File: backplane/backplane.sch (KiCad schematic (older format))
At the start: 57 parts, among them J1 Conn_PCB1, J10 Conn_SSR_INPUT, J12 Conn_SSR_PCB2, J13 Conn_01x05, J14 LCD_MCU_CONNECTOR, J15 Screw_Terminal_AQ_2, J16 Screw_Terminal_AQ_1, J17 Screw_Terminal_O3_1, J18 Conn_TO_ION_AIR, J19 Conn_01x08, J2 Conn_PCB2, J20 FAN_CONNECTOR, J21 PERFUME_CONNECTOR, J22 LED_STRIP_CONNECTOR, J23 PCB1_COMM_CONNECTOR, J24 Conn_01x08, J25 PCB1_ALARM, J26 CONNECTOR, J27 UART2, J28 TEST, J29 UART3, J3 Conn_FAN_48V_SOURCE, J30 CONNECTOR, J31 LCD_MCU_CONNECTOR, J32 UART2, J33 UART3, J34 232_TEST_POINT, J35 UART_TEST_POINT, J36 MCU_UART_TEST_POINT, J37 FAN_TEST_POINT, J4 CONNECTOR, J5 Conn_SSR_POWER_SOURCE, J6 Conn_MCU_5V_SOURCE, J7 Conn_humidity_sensor_terminal, J8 Conn_flow_sensor_terminal, J9 Conn_SSR_5V_INPUT, Q4 2n3904, Q5 2n3904, Q6 2n3904, U1 BLUEPILL, U2 MAX3232_MODULE

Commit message: remove uart, 232 circuit,
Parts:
- removed D1, D2, D3, D5: LED, LED_THT:LED_D3.0mm_Clear, symbol Device:LED
- removed J32: UART2, backplate:PhoenixContact_MCV_1,5_2-G-3.5_1x02_P3.50mm_Vertical_handsolder, symbol bluepill:Conn_01x02
- removed J33: UART3, backplate:PhoenixContact_MCV_1,5_2-G-3.5_1x03_P3.50mm_Vertical_handsolder, symbol bluepill:Conn_01x03
- removed J34: 232_TEST_POINT, backplate:Pin_Header_Straight_1x02_Pitch2.54mm, symbol bluepill:Conn_01x02
- removed J35: UART_TEST_POINT, backplate:Pin_Header_Straight_1x02_Pitch2.54mm, symbol bluepill:Conn_01x02
- removed J36: MCU_UART_TEST_POINT, backplate:Pin_Header_Straight_1x02_Pitch2.54mm, symbol bluepill:Conn_01x02
- removed Q4, Q5, Q6: 2n3904, backplate:TO-92L_HandSolder, symbol Transistor_BJT:2N3904
- removed R11, R7, R8, R9: 330, backplate:R_1206_3216Metric_Pad1.42x1.75mm_HandSolder, symbol Device:R
- removed R12, R13, R14: 120, backplate:R_1206_3216Metric_Pad1.42x1.75mm_HandSolder, symbol Device:R
- removed R15, R16, R17: 0, backplate:R_1206_3216Metric_Pad1.42x1.75mm_HandSolder, symbol Device:R
- removed U2: MAX3232_MODULE, backplate:MAX3232_MOEULE_handsolder, symbol bluepill:MAX3232_MODULE
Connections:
- wire segments 299 -> 233

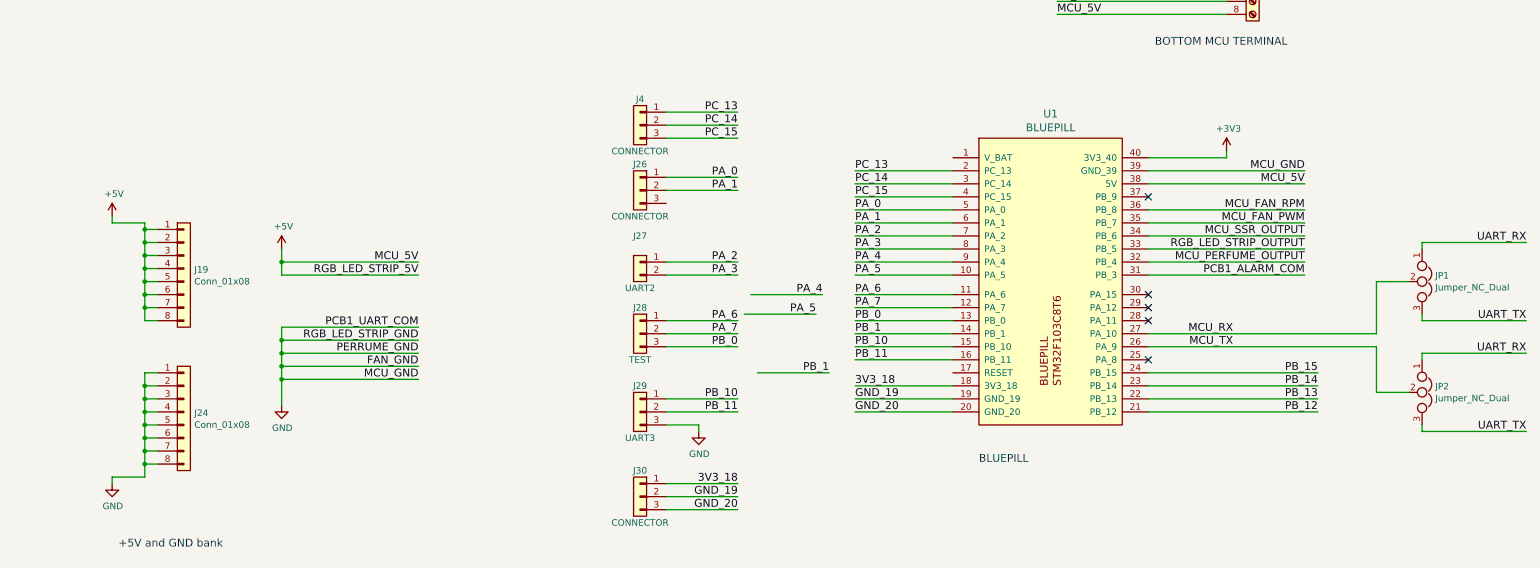
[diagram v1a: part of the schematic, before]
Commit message: remove stm32,
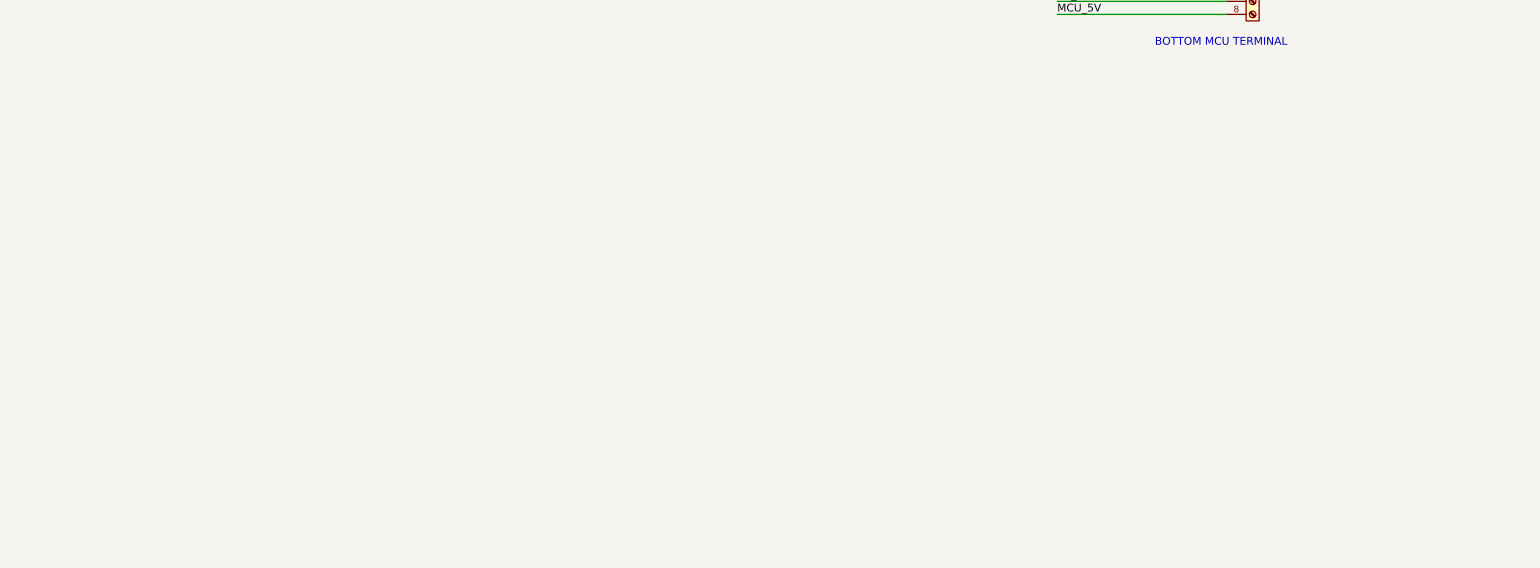
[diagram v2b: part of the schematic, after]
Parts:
- removed J19, J24: Conn_01x08, backplate:PinHeader_1x08_P2.54mm_Vertical_handsolder, symbol Connector_Generic:Conn_01x08
- removed J26, J30, J4: CONNECTOR, backplate:PhoenixContact_MCV_1,5_2-G-3.5_1x03_P3.50mm_Vertical_handsolder, symbol bluepill:Conn_01x03
- removed J27: UART2, backplate:PhoenixContact_MCV_1,5_2-G-3.5_1x02_P3.50mm_Vertical_handsolder, symbol bluepill:Conn_01x02
- removed J28: TEST, backplate:PhoenixContact_MCV_1,5_2-G-3.5_1x03_P3.50mm_Vertical_handsolder, symbol bluepill:Conn_01x03
- removed J29: UART3, backplate:PhoenixContact_MCV_1,5_2-G-3.5_1x03_P3.50mm_Vertical_handsolder, symbol bluepill:Conn_01x03
- removed JP1, JP2: Jumper_NC_Dual, backplate:SolderJumper-3_P1.3mm_Open_RoundedPad1.0x1.5mm, symbol Device:Jumper_NC_Dual
- removed U1: BLUEPILL, backplate:DIP-40_W15.24mm_Socket_LongPads_handsolder, symbol bluepill:BLUEPILL
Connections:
- net +5V: no longer J14.8 (Pin_8), J22.1 (Pin_1), J31.8 (Pin_8), J6.1 (Pin_1)
- net GND: no longer J14.1 (Pin_1), J20.2 (Pin_2), J21.2 (Pin_2), J22.3 (Pin_3), J23.1 (Pin_1), J3.2 (Pin_2), J31.1 (Pin_1), J37.2 (Pin_2), J6.2 (Pin_2)
- new net FAN_GND: J20.2 (Pin_2), J3.2 (Pin_2), J37.2 (Pin_2)
- new net MCU_5V: J14.8 (Pin_8), J31.8 (Pin_8), J6.1 (Pin_1)
- new net MCU_GND: J14.1 (Pin_1), J31.1 (Pin_1), J6.2 (Pin_2)
- new net PCB1_UART_COM: J23.1 (Pin_1)
- new net PERRUME_GND: J21.2 (Pin_2)
- new net RGB_LED_STRIP_5V: J22.1 (Pin_1)
- new net RGB_LED_STRIP_GND: J22.3 (Pin_3)
- no-connect marks 6 -> 1
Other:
- note removed: "+5V and GND bank"
- note removed: "BLUEPILL"

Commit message: remove stm32,
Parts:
- removed J14: LCD_MCU_CONNECTOR, backplate:TE_84952-8_1x08-1MP_P1.0mm_Horizontal, symbol Connector_Generic:Conn_01x08
- removed J20: FAN_CONNECTOR, backplate:PhoenixContact_MCV_1,5_4-G-3.5_1x04_P3.50mm_Vertical_handsolder, symbol Connector_Generic:Conn_01x04
- removed J21: PERFUME_CONNECTOR, backplate:PhoenixContact_MCV_1,5_2-G-3.5_1x02_P3.50mm_Vertical_handsolder, symbol bluepill:Conn_01x02
- removed J22: LED_STRIP_CONNECTOR, backplate:PhoenixContact_MCV_1,5_2-G-3.5_1x03_P3.50mm_Vertical_handsolder, symbol bluepill:Conn_01x03
- removed J3: Conn_FAN_48V_SOURCE, backplate:PhoenixContact_MCV_1,5_2-G-3.5_1x02_P3.50mm_Vertical_handsolder, symbol bluepill:Conn_01x02
- removed J31: LCD_MCU_CONNECTOR, backplate:PinHeader_1x08_P2.54mm_Vertical_handsolder, symbol Connector:Screw_Terminal_01x08
- removed J37: FAN_TEST_POINT, backplate:PhoenixContact_MCV_1,5_4-G-3.5_1x04_P3.50mm_Vertical_handsolder, symbol Connector_Generic:Conn_01x04
- removed J6: Conn_MCU_5V_SOURCE, backplate:PhoenixContact_MCV_1,5_2-G-3.5_1x02_P3.50mm_Vertical_handsolder, symbol bluepill:Conn_01x02
- removed J7: Conn_humidity_sensor_terminal, backplate:PhoenixContact_MCV_1,5_2-G-3.5_1x02_P3.50mm_Vertical_handsolder, symbol bluepill:Conn_01x02
- removed J8: Conn_flow_sensor_terminal, backplate:PhoenixContact_MCV_1,5_2-G-3.5_1x03_P3.50mm_Vertical_handsolder, symbol bluepill:Conn_01x03
- removed J9: Conn_SSR_5V_INPUT, backplate:PhoenixContact_MCV_1,5_2-G-3.5_1x02_P3.50mm_Vertical_handsolder, symbol bluepill:Conn_01x02
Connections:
- no-connect marks 1 -> 0
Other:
- note removed: "BOTTOM MCU TERMINAL"
- note removed: "connection between \noutside sensor wire and back plane"

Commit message: remove stm32,
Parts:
- added J3: Conn_SSR_INPUT, footprint-lib:mpt_0,5%2f2-2,54, symbol bluepill:Conn_01x02
- added J4: Conn_01x08, footprint-lib:s8b-ph-kl, symbol Connector_Generic:Conn_01x08
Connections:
- net PCB1_UART_COM is gone; now on net GND: J23.1 (Pin_1)
- net +5V: now also J4.8 (Pin_8)
- net GND: now also J4.1 (Pin_1)
- net PCB1_232_RX: now also J4.4 (Pin_4)
- net PCB1_232_TX: now also J4.5 (Pin_5)
- net PCB1_ALARM_COM: now also J4.6 (Pin_6)
- new net SSR-24-DA_N: J3.2 (Pin_2), J4.3 (Pin_3)
- new net SSR-24-DA_P: J3.1 (Pin_1), J4.2 (Pin_2)
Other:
- moved on the sheet: J1, J10, J12, J13, J15, J16, J17, J18, J2, J23, J25, J5

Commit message: update,
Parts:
- J13: footprint backplate:PhoenixContact_MCV_1,5_8-G-3.5_1x05_P3.50mm_Vertical_handsolder -> footprint-lib:mpt_0,5%2f5-2,54
- J16, J17: footprint backplate:PhoenixContact_MCV_1,5_4-G-3.5_1x04_P3.50mm_Vertical_handsolder -> footprint-lib:mpt_0,5%2f4-2,54
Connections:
- net AQ1_5V: now also J16.3 (Pin_3); no longer J16.2 (Pin_2)
- net AQ1_GND: now also J16.4 (Pin_4); no longer J16.1 (Pin_1)
- net AQ1_SENSOR: now also J16.2 (Pin_2); no longer J16.3 (Pin_3)
- net AQ1_SHIELD: now also J16.1 (Pin_1); no longer J16.4 (Pin_4)
- net O3_1_24V: now also J17.3 (Pin_3); no longer J17.2 (Pin_2)
- net O3_1_GND: now also J17.4 (Pin_4); no longer J17.1 (Pin_1)
- net O3_1_SENSOR: now also J17.2 (Pin_2); no longer J17.3 (Pin_3)
- net O3_1_SHIELD: now also J17.1 (Pin_1); no longer J17.4 (Pin_4)
- net flow_sensor_%RH: now also J13.4 (Pin_4); no longer J13.2 (Pin_2)
- net flow_sensor_24V: now also J13.2 (Pin_2); no longer J13.4 (Pin_4)
- net flow_sensor_GND: now also J13.1 (Pin_1); no longer J13.5 (Pin_5)
- net flow_sensor_shield: now also J13.5 (Pin_5); no longer J13.1 (Pin_1)
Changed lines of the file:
@@
 L bluepill:Screw_Terminal_01x04 J16
 U 1 1 5B60002E
-P 1650 6350
-F 0 "J16" H 1650 6550 50  0000 C CNN
-F 1 "Screw_Terminal_AQ_1" H 1650 6050 50  0000 C CNN
-F 2 "backplate:PhoenixContact_MCV_1,5_4-G-3.5_1x04_P3.50mm_Vertical_handsolder" H 1650 6350 50  0001 C CNN
-F 3 "" H 1650 6350 50  0001 C CNN
-	1    1650 6350
-	-1   0    0    -1
+P 1650 6450
+F 0 "J16" H 1650 6650 50  0000 C CNN
+F 1 "Screw_Terminal_AQ_1" H 1650 6150 50  0000 C CNN
+F 2 "footprint-lib:mpt_0,5%2f4-2,54" H 1650 6450 50  0001 C CNN
+F 3 "" H 1650 6450 50  0001 C CNN
+	1    1650 6450
+	-1   0    0    1
 $EndComp
 Text Label 2550 6350 2    60   ~ 0
@@
 L bluepill:Screw_Terminal_01x04 J17
 U 1 1 5B600434
-P 1650 7100
-F 0 "J17" H 1650 7300 50  0000 C CNN
-F 1 "Screw_Terminal_O3_1" H 1650 6800 50  0000 C CNN
-F 2 "backplate:PhoenixContact_MCV_1,5_4-G-3.5_1x04_P3.50mm_Vertical_handsolder" H 1650 7100 50  0001 C CNN
-F 3 "" H 1650 7100 50  0001 C CNN
-	1    1650 7100
-	-1   0    0    -1
+P 1650 7200
+F 0 "J17" H 1650 7400 50  0000 C CNN
+F 1 "Screw_Terminal_O3_1" H 1650 6900 50  0000 C CNN
+F 2 "footprint-lib:mpt_0,5%2f4-2,54" H 1650 7200 50  0001 C CNN
+F 3 "" H 1650 7200 50  0001 C CNN
+	1    1650 7200
+	-1   0    0    1
 $EndComp
 Text Label 2550 7100 2    60   ~ 0
@@
 F 0 "J13" H 4020 1667 50  0000 C CNN
 F 1 "Conn_01x05" H 4020 1576 50  0000 C CNN
-F 2 "backplate:PhoenixContact_MCV_1,5_8-G-3.5_1x05_P3.50mm_Vertical_handsolder" H 4100 1250 50  0001 C CNN
+F 2 "footprint-lib:mpt_0,5%2f5-2,54" H 4100 1250 50  0001 C CNN
 F 3 "~" H 4100 1250 50  0001 C CNN
 	1    4100 1250
-	-1   0    0    -1
+	-1   0    0    1
 $EndComp
 Text Label 5350 1050 2    60   ~ 0

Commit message: update,
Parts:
- J13: value Conn_01x05 -> FLOW_SENSOR
- J15: value Screw_Terminal_AQ_2 -> AQ2_SENSOR; footprint backplate:Pin_Header_Straight_1x04_Pitch2.54mm -> footprint-lib:mpt_0,5%2f4-2,54
- J16: value Screw_Terminal_AQ_1 -> AQ1_SENSOR
- J17: value Screw_Terminal_O3_1 -> O3_SENSOR
- J3: value Conn_SSR_INPUT -> SSR_CONTROL
- J4: value Conn_01x08 -> TO_CONTROL_BOARD
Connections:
- net AQ2_5V: now also J15.2 (Pin_2); no longer J15.3 (Pin_3)
- net AQ2_GND: now also J15.1 (Pin_1); no longer J15.4 (Pin_4)
- net AQ2_SENSOR: now also J15.3 (Pin_3); no longer J15.2 (Pin_2)
- net AQ2_SHIELD: now also J15.4 (Pin_4); no longer J15.1 (Pin_1)
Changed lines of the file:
@@
 L bluepill:Screw_Terminal_01x04 J15
 U 1 1 5B5FFAB1
-P 1650 5650
-F 0 "J15" H 1650 5850 50  0000 C CNN
-F 1 "Screw_Terminal_AQ_2" H 1650 5350 50  0000 C CNN
-F 2 "backplate:Pin_Header_Straight_1x04_Pitch2.54mm" H 1650 5650 50  0001 C CNN
-F 3 "" H 1650 5650 50  0001 C CNN
-	1    1650 5650
-	-1   0    0    -1
+P 1650 5750
+F 0 "J15" H 1650 5950 50  0000 C CNN
+F 1 "AQ2_SENSOR" H 1650 5450 50  0000 C CNN
+F 2 "footprint-lib:mpt_0,5%2f4-2,54" H 1650 5750 50  0001 C CNN
+F 3 "" H 1650 5750 50  0001 C CNN
+	1    1650 5750
+	-1   0    0    1
 $EndComp
 Text Label 2550 5750 2    60   ~ 0
@@
 P 1650 6450
 F 0 "J16" H 1650 6650 50  0000 C CNN
-F 1 "Screw_Terminal_AQ_1" H 1650 6150 50  0000 C CNN
+F 1 "AQ1_SENSOR" H 1650 6150 50  0000 C CNN
 F 2 "footprint-lib:mpt_0,5%2f4-2,54" H 1650 6450 50  0001 C CNN
 F 3 "" H 1650 6450 50  0001 C CNN
@@
 P 1650 7200
 F 0 "J17" H 1650 7400 50  0000 C CNN
-F 1 "Screw_Terminal_O3_1" H 1650 6900 50  0000 C CNN
+F 1 "O3_SENSOR" H 1650 6900 50  0000 C CNN
 F 2 "footprint-lib:mpt_0,5%2f4-2,54" H 1650 7200 50  0001 C CNN
 F 3 "" H 1650 7200 50  0001 C CNN
@@
 P 4100 1250
 F 0 "J13" H 4020 1667 50  0000 C CNN
-F 1 "Conn_01x05" H 4020 1576 50  0000 C CNN
+F 1 "FLOW_SENSOR" H 4020 1576 50  0000 C CNN
 F 2 "footprint-lib:mpt_0,5%2f5-2,54" H 4100 1250 50  0001 C CNN
 F 3 "~" H 4100 1250 50  0001 C CNN
@@
 P 10200 3200
 F 0 "J4" H 10280 3192 50  0000 L CNN
-F 1 "Conn_01x08" H 10280 3101 50  0000 L CNN
+F 1 "TO_CONTROL_BOARD" H 10280 3101 50  0000 L CNN
 F 2 "footprint-lib:s8b-ph-kl" H 10200 3200 50  0001 C CNN
 F 3 "~" H 10200 3200 50  0001 C CNN
@@
 P 6350 2900
 F 0 "J3" H 6350 3000 50  0000 C CNN
-F 1 "Conn_SSR_INPUT" H 6350 2700 50  0000 C CNN
+F 1 "SSR_CONTROL" H 6350 2700 50  0000 C CNN
 F 2 "footprint-lib:mpt_0,5%2f2-2,54" H 6350 2900 50  0001 C CNN
 F 3 "" H 6350 2900 50  0001 C CNN

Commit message: update board mounting hole,
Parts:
- added H? (x4): PCB2, MountingHole:MountingHole_3.2mm_M3_DIN965, symbol Mechanical:MountingHole
- added H? (x5): PCB1, MountingHole:MountingHole_3.2mm_M3_DIN965, symbol Mechanical:MountingHole
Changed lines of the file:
@@
 Wire Wire Line
 	6550 2200 7850 2200
+$Comp
+L Mechanical:MountingHole H?
+U 1 1 5BE6E1EE
+P 7750 4950
+F 0 "H?" H 7850 4996 50  0000 L CNN
+F 1 "PCB2" H 7850 4905 50  0000 L CNN
+F 2 "MountingHole:MountingHole_3.2mm_M3_DIN965" H 7750 4950 50  0001 C CNN
+F 3 "~" H 7750 4950 50  0001 C CNN
+	1    7750 4950
+	1    0    0    -1
+$EndComp
+$Comp
+L Mechanical:MountingHole H?
+U 1 1 5BE6E3BE
+P 7750 5150
+F 0 "H?" H 7850 5196 50  0000 L CNN
+F 1 "PCB2" H 7850 5105 50  0000 L CNN
+F 2 "MountingHole:MountingHole_3.2mm_M3_DIN965" H 7750 5150 50  0001 C CNN
+F 3 "~" H 7750 5150 50  0001 C CNN
+	1    7750 5150
+	1    0    0    -1
+$EndComp
+$Comp
+L Mechanical:MountingHole H?
+U 1 1 5BE6E3F6
+P 7750 5350
+F 0 "H?" H 7850 5396 50  0000 L CNN
+F 1 "PCB2" H 7850 5305 50  0000 L CNN
+F 2 "MountingHole:MountingHole_3.2mm_M3_DIN965" H 7750 5350 50  0001 C CNN
+F 3 "~" H 7750 5350 50  0001 C CNN
+	1    7750 5350
+	1    0    0    -1
+$EndComp
+$Comp
+L Mechanical:MountingHole H?
+U 1 1 5BE6E42C
+P 7750 5550
+F 0 "H?" H 7850 5596 50  0000 L CNN
+F 1 "PCB2" H 7850 5505 50  0000 L CNN
+F 2 "MountingHole:MountingHole_3.2mm_M3_DIN965" H 7750 5550 50  0001 C CNN
+F 3 "~" H 7750 5550 50  0001 C CNN
+	1    7750 5550
+	1    0    0    -1
+$EndComp
+$Comp
+L Mechanical:MountingHole H?
+U 1 1 5BE6E69F
+P 8500 4950
+F 0 "H?" H 8600 4996 50  0000 L CNN
+F 1 "PCB1" H 8600 4905 50  0000 L CNN
+F 2 "MountingHole:MountingHole_3.2mm_M3_DIN965" H 8500 4950 50  0001 C CNN
+F 3 "~" H 8500 4950 50  0001 C CNN
+	1    8500 4950
+	1    0    0    -1
+$EndComp
+$Comp
+L Mechanical:MountingHole H?
+U 1 1 5BE74A69
+P 8500 5150
+F 0 "H?" H 8600 5196 50  0000 L CNN
+F 1 "PCB1" H 8600 5105 50  0000 L CNN
+F 2 "MountingHole:MountingHole_3.2mm_M3_DIN965" H 8500 5150 50  0001 C CNN
+F 3 "~" H 8500 5150 50  0001 C CNN
+	1    8500 5150
+	1    0    0    -1
+$EndComp
+$Comp
+L Mechanical:MountingHole H?
+U 1 1 5BE77C40
+P 8500 5350
+F 0 "H?" H 8600 5396 50  0000 L CNN
+F 1 "PCB1" H 8600 5305 50  0000 L CNN
+F 2 "MountingHole:MountingHole_3.2mm_M3_DIN965" H 8500 5350 50  0001 C CNN
+F 3 "~" H 8500 5350 50  0001 C CNN
+	1    8500 5350
+	1    0    0    -1
+$EndComp
+$Comp
+L Mechanical:MountingHole H?
+U 1 1 5BE77C46
+P 8500 5550
+F 0 "H?" H 8600 5596 50  0000 L CNN
+F 1 "PCB1" H 8600 5505 50  0000 L CNN
+F 2 "MountingHole:MountingHole_3.2mm_M3_DIN965" H 8500 5550 50  0001 C CNN
+F 3 "~" H 8500 5550 50  0001 C CNN
+	1    8500 5550
+	1    0    0    -1
+$EndComp
+$Comp
+L Mechanical:MountingHole H?
+U 1 1 5BE7ADFF
+P 8500 5750
+F 0 "H?" H 8600 5796 50  0000 L CNN
+F 1 "PCB1" H 8600 5705 50  0000 L CNN
+F 2 "MountingHole:MountingHole_3.2mm_M3_DIN965" H 8500 5750 50  0001 C CNN
+F 3 "~" H 8500 5750 50  0001 C CNN
+	1    8500 5750
+	1    0    0    -1
+$EndComp
 $EndSCHEMATC
